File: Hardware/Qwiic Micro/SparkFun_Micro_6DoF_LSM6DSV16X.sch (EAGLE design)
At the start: 29 parts, among them J1 Qwiic Right Angle, U2 LSM6DSV16X

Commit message: Adds proto gerbers
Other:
- note added: "v01"
- note removed: "v10"
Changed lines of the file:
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@@
 <text x="65.786" y="172.974" size="1.27" layer="97" font="vector">VDD Range: 1.71V - 3.6V
 VDDIO Range: 1.62V - 3.6V</text>
-<text x="238.76" y="7.62" size="2.54" layer="94" font="vector">v10</text>
+<text x="238.76" y="7.62" size="2.54" layer="94" font="vector">v01</text>
 <text x="210.82" y="180.34" size="2.54" layer="94" font="vector" align="center">Jumpers</text>
 <text x="213.36" y="132.08" size="1.778" layer="97" font="vector">Cut trace to

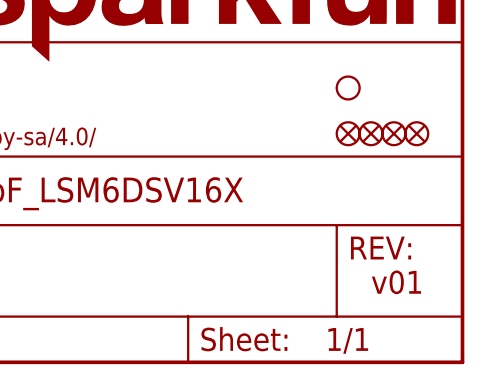
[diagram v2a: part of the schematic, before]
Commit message: Rolls version to v10 on Micro, increases the size of the pin one indicator for the LED
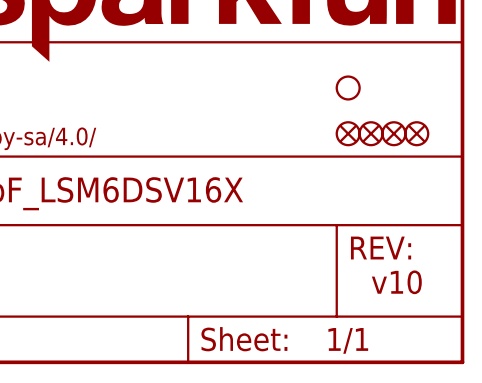
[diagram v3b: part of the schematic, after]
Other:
- note added: "v10"
- note removed: "v01"
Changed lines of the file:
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@@
 <text x="65.786" y="172.974" size="1.27" layer="97" font="vector">VDD Range: 1.71V - 3.6V
 VDDIO Range: 1.62V - 3.6V</text>
-<text x="238.76" y="7.62" size="2.54" layer="94" font="vector">v01</text>
+<text x="238.76" y="7.62" size="2.54" layer="94" font="vector">v10</text>
 <text x="210.82" y="180.34" size="2.54" layer="94" font="vector" align="center">Jumpers</text>
 <text x="213.36" y="132.08" size="1.778" layer="97" font="vector">Cut trace to

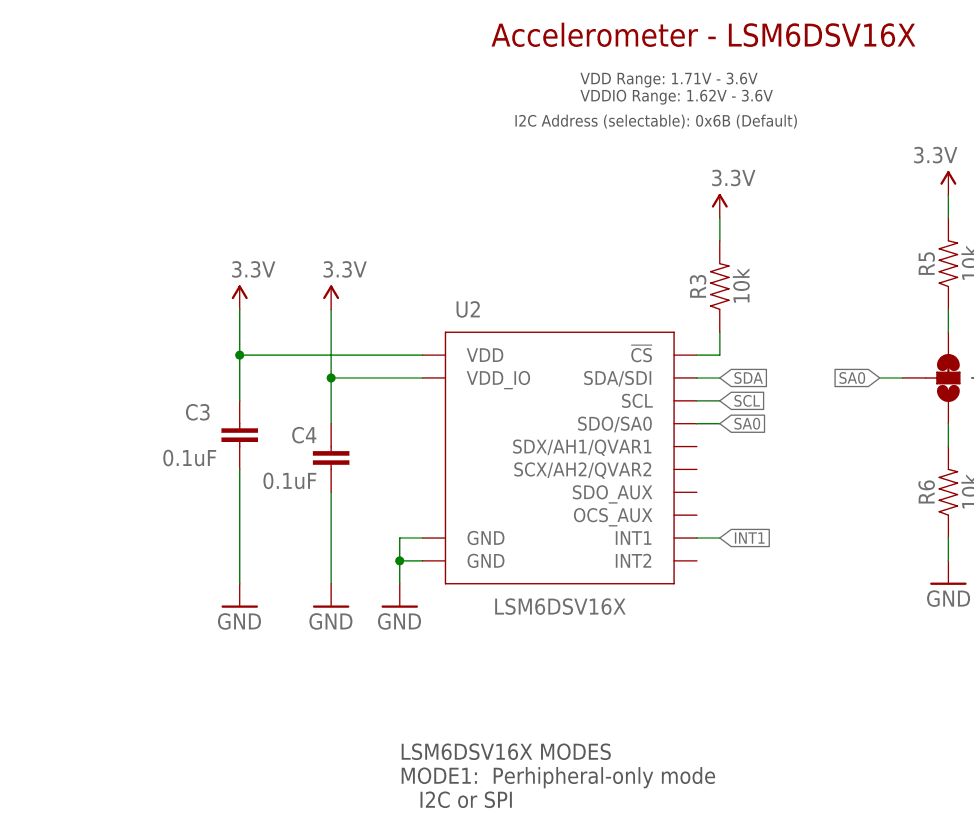
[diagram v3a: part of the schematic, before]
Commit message: Grounds SCx and SDx on  micro since they are not used
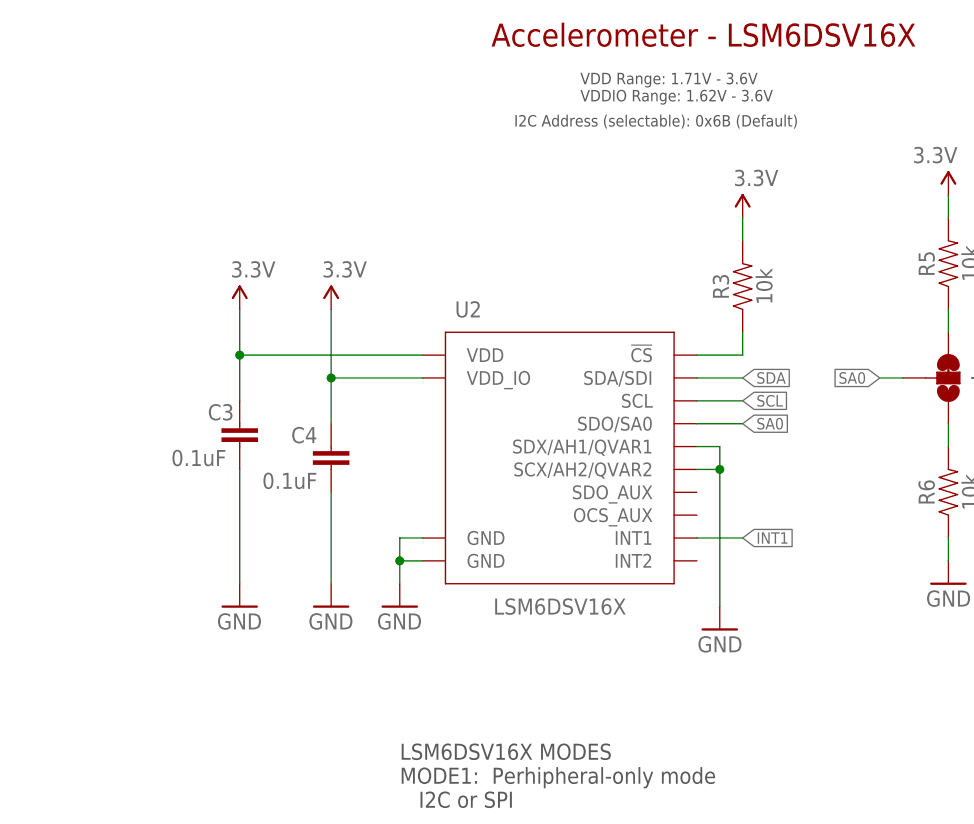
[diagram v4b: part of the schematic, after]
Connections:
- net GND: now also U2.SCX/AH2/QVAR2, U2.SDX/AH1/QVAR1
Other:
- moved on the sheet: R3
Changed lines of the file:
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@@
 <part name="SUPPLY7" library="SparkFun-PowerSymbols" deviceset="3.3V" device=""/>
 <part name="U2" library="lsm6dsv16x" deviceset="LSM6DSV16X" device=""/>
+<part name="GND8" library="SparkFun-PowerSymbols" deviceset="GND" device=""/>
 </parts>
 <sheets>
@@
 </instance>
 <instance part="C3" gate="G$1" x="27.94" y="134.62" smashed="yes">
-<attribute name="NAME" x="21.844" y="137.541" size="1.778" layer="95" font="vector"/>
-<attribute name="VALUE" x="19.304" y="132.461" size="1.778" layer="96" font="vector"/>
+<attribute name="NAME" x="24.384" y="137.541" size="1.778" layer="95" font="vector"/>
+<attribute name="VALUE" x="20.32" y="132.461" size="1.778" layer="96" font="vector"/>
 </instance>
 <instance part="ADDR" gate="G$1" x="106.68" y="142.24" smashed="yes" rot="MR180">
@@
 <attribute name="VALUE" x="139.7" y="86.36" size="1.778" layer="96" font="vector"/>
 </instance>
-<instance part="R3" gate="G$1" x="81.28" y="152.4" smashed="yes" rot="R90">
-<attribute name="NAME" x="79.756" y="152.4" size="1.778" layer="95" font="vector" rot="R90" align="bottom-center"/>
-<attribute name="VALUE" x="82.804" y="152.4" size="1.778" layer="96" font="vector" rot="R90" align="top-center"/>
-</instance>
-<instance part="SUPPLY7" gate="G$1" x="81.28" y="160.02" smashed="yes">
-<attribute name="VALUE" x="80.264" y="163.576" size="1.778" layer="96" font="vector"/>
+<instance part="R3" gate="G$1" x="83.82" y="152.4" smashed="yes" rot="R90">
+<attribute name="NAME" x="82.296" y="152.4" size="1.778" layer="95" font="vector" rot="R90" align="bottom-center"/>
+<attribute name="VALUE" x="85.344" y="152.4" size="1.778" layer="96" font="vector" rot="R90" align="top-center"/>
+</instance>
+<instance part="SUPPLY7" gate="G$1" x="83.82" y="160.02" smashed="yes">
+<attribute name="VALUE" x="82.804" y="163.576" size="1.778" layer="96" font="vector"/>
 </instance>
 <instance part="U2" gate="G$1" x="63.5" y="134.62" smashed="yes">
 <attribute name="NAME" x="53.34" y="149.86" size="1.778" layer="95" font="vector" align="center"/>
 <attribute name="VALUE" x="63.5" y="116.84" size="1.778" layer="96" font="vector" align="center"/>
+</instance>
+<instance part="GND8" gate="1" x="81.28" y="114.3" smashed="yes" rot="MR0">
+<attribute name="VALUE" x="83.82" y="111.76" size="1.778" layer="96" font="vector" rot="MR0"/>
 </instance>
 </instances>
@@
 <pinref part="GND1" gate="1" pin="GND"/>
 </segment>
+<segment>
+<pinref part="U2" gate="G$1" pin="SDX/AH1/QVAR1"/>
+<wire x1="78.74" y1="134.62" x2="81.28" y2="134.62" width="0.1524" layer="91"/>
+<wire x1="81.28" y1="134.62" x2="81.28" y2="132.08" width="0.1524" layer="91"/>
+<pinref part="U2" gate="G$1" pin="SCX/AH2/QVAR2"/>
+<wire x1="78.74" y1="132.08" x2="81.28" y2="132.08" width="0.1524" layer="91"/>
+<junction x="81.28" y="132.08"/>
+<wire x1="81.28" y1="132.08" x2="81.28" y2="116.84" width="0.1524" layer="91"/>
+<pinref part="GND8" gate="1" pin="GND"/>
+</segment>
 </net>
 <net name="SCL" class="0">
 <segment>
-<wire x1="78.74" y1="139.7" x2="81.28" y2="139.7" width="0.1524" layer="91"/>
-<label x="81.28" y="139.7" size="1.27" layer="95" font="vector" xref="yes"/>
+<wire x1="78.74" y1="139.7" x2="83.82" y2="139.7" width="0.1524" layer="91"/>
+<label x="83.82" y="139.7" size="1.27" layer="95" font="vector" xref="yes"/>
 <pinref part="U2" gate="G$1" pin="SCL"/>
 </segment>
@@
 <net name="SDA" class="0">
 <segment>
-<wire x1="78.74" y1="142.24" x2="81.28" y2="142.24" width="0.1524" layer="91"/>
-<label x="81.28" y="142.24" size="1.27" layer="95" font="vector" xref="yes"/>
+<wire x1="78.74" y1="142.24" x2="83.82" y2="142.24" width="0.1524" layer="91"/>
+<label x="83.82" y="142.24" size="1.27" layer="95" font="vector" xref="yes"/>
 <pinref part="U2" gate="G$1" pin="SDA/SDI"/>
 </segment>
@@
 <net name="SA0" class="0">
 <segment>
-<wire x1="78.74" y1="137.16" x2="81.28" y2="137.16" width="0.1524" layer="91"/>
-<label x="81.28" y="137.16" size="1.27" layer="95" font="vector" xref="yes"/>
+<wire x1="78.74" y1="137.16" x2="83.82" y2="137.16" width="0.1524" layer="91"/>
+<label x="83.82" y="137.16" size="1.27" layer="95" font="vector" xref="yes"/>
 <pinref part="U2" gate="G$1" pin="SDO/SA0"/>
 </segment>
@@
 <net name="INT1" class="0">
 <segment>
-<wire x1="81.28" y1="124.46" x2="78.74" y2="124.46" width="0.1524" layer="91"/>
-<label x="81.28" y="124.46" size="1.27" layer="95" font="vector" xref="yes"/>
+<wire x1="83.82" y1="124.46" x2="78.74" y2="124.46" width="0.1524" layer="91"/>
+<label x="83.82" y="124.46" size="1.27" layer="95" font="vector" xref="yes"/>
 <pinref part="U2" gate="G$1" pin="INT1"/>
 </segment>
@@
 <pinref part="R3" gate="G$1" pin="2"/>
 <pinref part="SUPPLY7" gate="G$1" pin="3.3V"/>
-<wire x1="81.28" y1="160.02" x2="81.28" y2="157.48" width="0.1524" layer="91"/>
+<wire x1="83.82" y1="160.02" x2="83.82" y2="157.48" width="0.1524" layer="91"/>
 </segment>
 <segment>
@@
 <net name="N$4" class="0">
 <segment>
-<wire x1="78.74" y1="144.78" x2="81.28" y2="144.78" width="0.1524" layer="91"/>
-<wire x1="81.28" y1="144.78" x2="81.28" y2="147.32" width="0.1524" layer="91"/>
+<wire x1="78.74" y1="144.78" x2="83.82" y2="144.78" width="0.1524" layer="91"/>
+<wire x1="83.82" y1="144.78" x2="83.82" y2="147.32" width="0.1524" layer="91"/>
 <pinref part="R3" gate="G$1" pin="1"/>
 <pinref part="U2" gate="G$1" pin="!CS!"/>
